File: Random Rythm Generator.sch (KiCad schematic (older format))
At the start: 24 parts, among them SW1 Randomise, U1 LM78L05_TO92, U2 40106, U3 4040, U4 74LS165

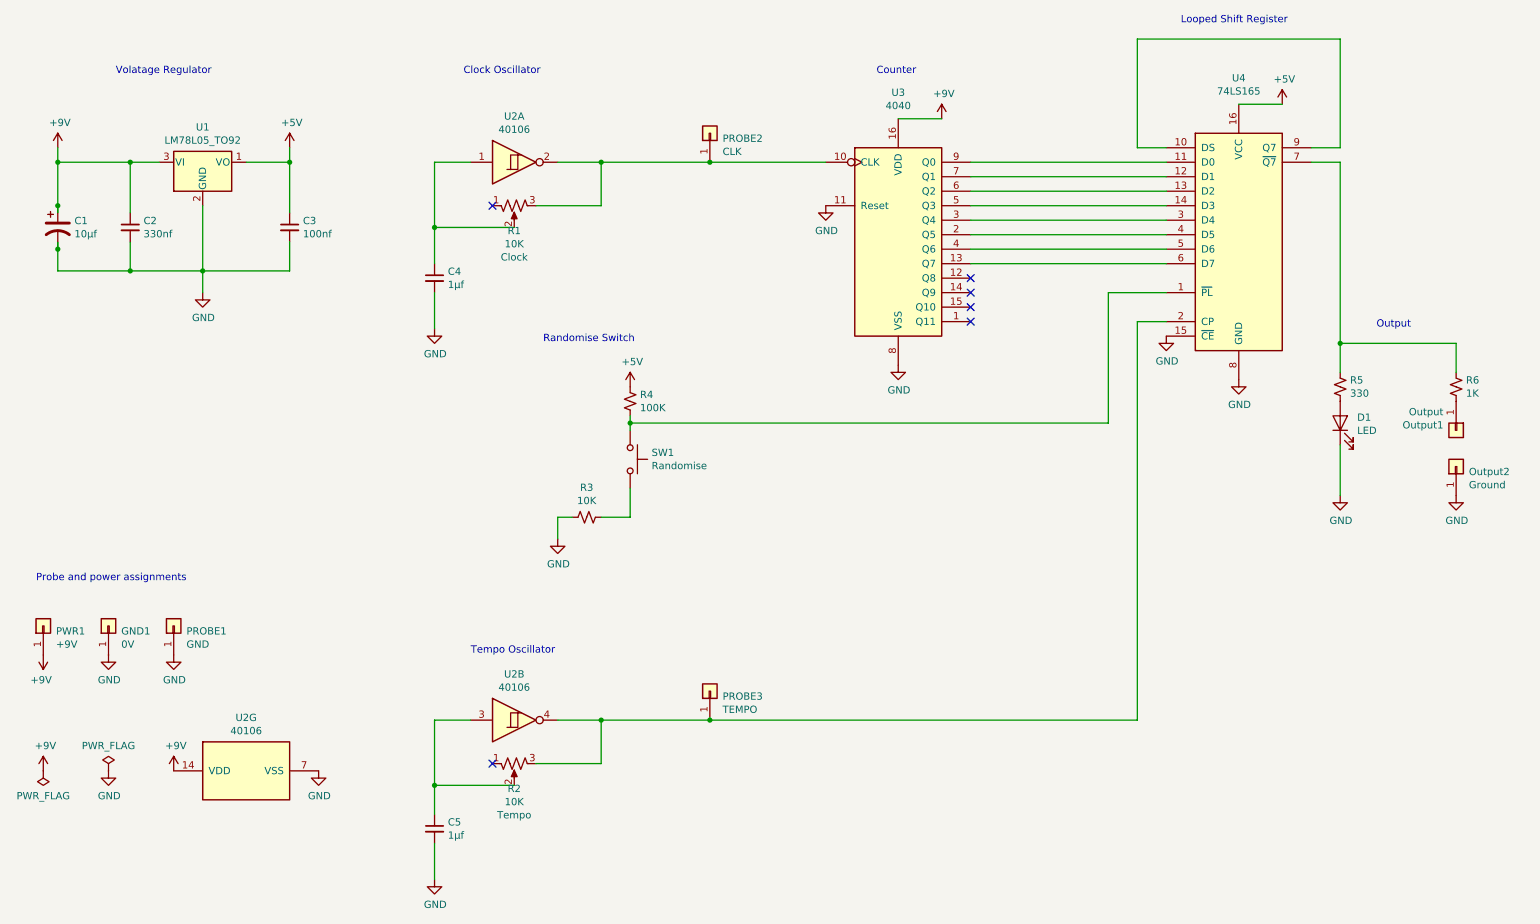
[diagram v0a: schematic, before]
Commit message: add output pins
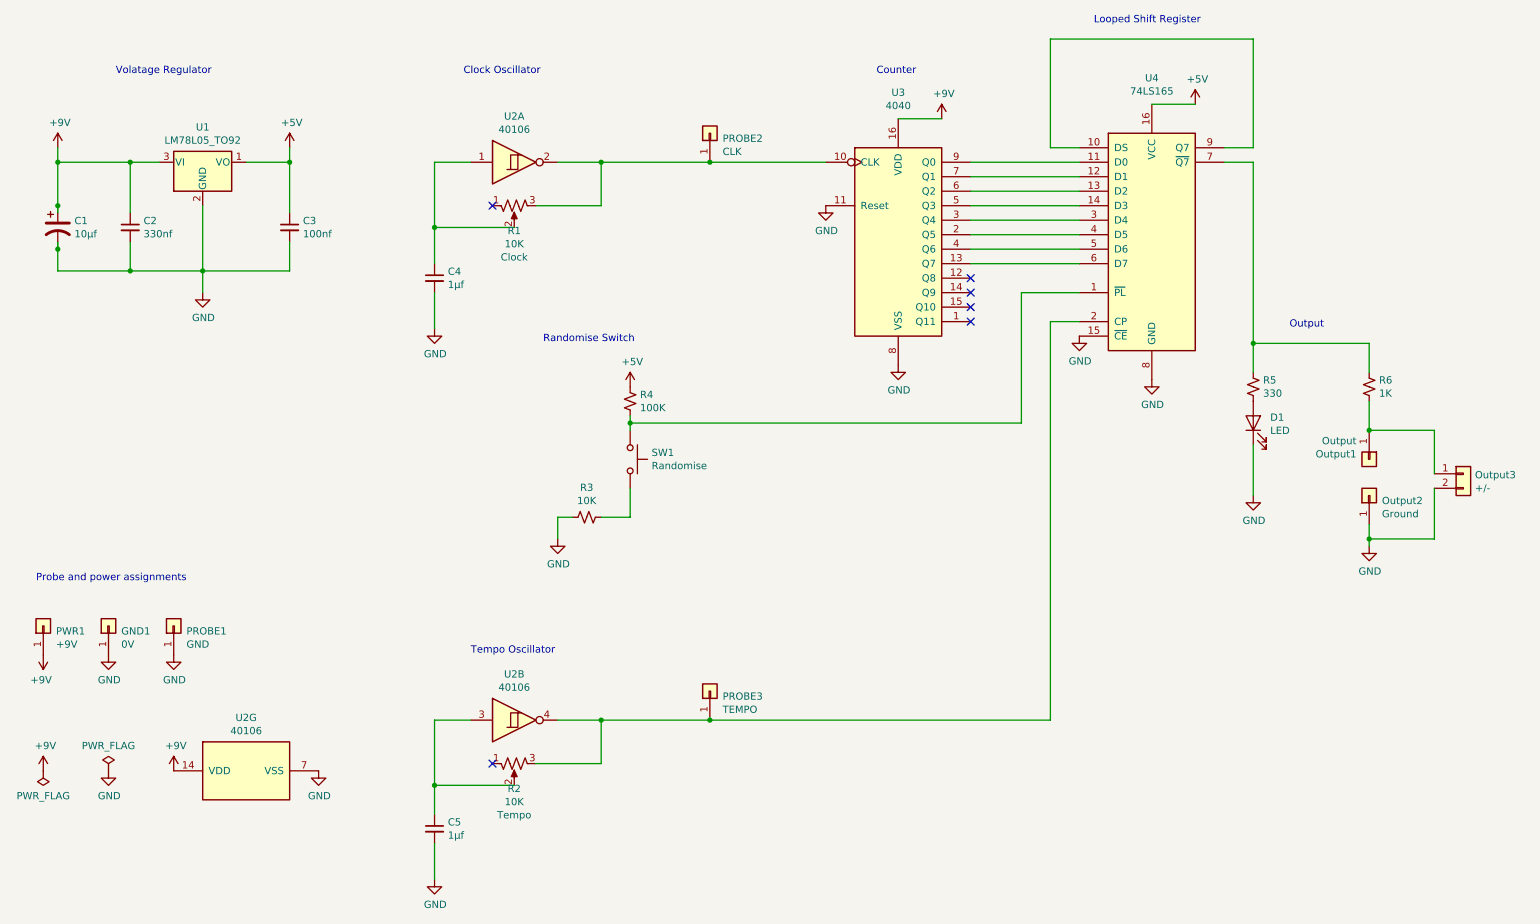
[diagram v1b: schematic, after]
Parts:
- added Output3: +/-, Connector_PinHeader_2.54mm:PinHeader_1x02_P2.54mm_Vertical, symbol Connector_Generic:Conn_01x02
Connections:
- wire segments 70 -> 77
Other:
- moved on the sheet: D1, Output1, Output2, R5, R6, U4
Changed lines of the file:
@@
 	3550 6650 3550 6900
 Wire Wire Line
-	7250 1950 8600 1950
-Wire Wire Line
-	8600 2050 7250 2050
-Wire Wire Line
-	7250 2150 8600 2150
-Wire Wire Line
-	7250 2250 8600 2250
-Wire Wire Line
-	8600 2350 7250 2350
-Wire Wire Line
-	8600 2550 7250 2550
-Wire Wire Line
-	7250 2650 8600 2650
+	7250 1950 8000 1950
+Wire Wire Line
+	8000 2050 7250 2050
+Wire Wire Line
+	7250 2150 8000 2150
+Wire Wire Line
+	7250 2250 8000 2250
+Wire Wire Line
+	8000 2350 7250 2350
+Wire Wire Line
+	8000 2550 7250 2550
+Wire Wire Line
+	7250 2650 8000 2650
 $Comp
 L power:+5V #PWR020
 U 1 1 5D24E019
-P 9400 1550
-F 0 "#PWR020" H 9400 1400 50  0001 C CNN
-F 1 "+5V" H 9415 1723 50  0000 C CNN
-F 2 "" H 9400 1550 50  0001 C CNN
-F 3 "" H 9400 1550 50  0001 C CNN
-	1    9400 1550
-	1    0    0    -1
-$EndComp
-Wire Wire Line
-	9100 1550 9400 1550
+P 8800 1550
+F 0 "#PWR020" H 8800 1400 50  0001 C CNN
+F 1 "+5V" H 8815 1723 50  0000 C CNN
+F 2 "" H 8800 1550 50  0001 C CNN
+F 3 "" H 8800 1550 50  0001 C CNN
+	1    8800 1550
+	1    0    0    -1
+$EndComp
+Wire Wire Line
+	8500 1550 8800 1550
 Wire Wire Line
 	6250 1950 5450 1950
@@
 	4900 4400 4700 4400
 Wire Wire Line
-	8200 2850 8600 2850
-Wire Wire Line
-	8600 3050 8400 3050
-Wire Wire Line
-	8400 3050 8400 5800
-Wire Wire Line
-	8400 5800 5450 5800
+	7600 2850 8000 2850
+Wire Wire Line
+	8000 3050 7800 3050
+Wire Wire Line
+	7800 3050 7800 5800
+Wire Wire Line
+	7800 5800 5450 5800
 Connection ~ 4700 5800
 $Comp
 L 74xx:74LS165 U4
 U 1 1 5D23B4A8
-P 9100 2450
-F 0 "U4" H 9100 3531 50  0000 C CNN
-F 1 "74LS165" H 9100 3440 50  0000 C CNN
-F 2 "Package_DIP:DIP-16_W7.62mm" H 9100 2450 50  0001 C CNN
-F 3 "http://www.ti.com/lit/gpn/sn74LS165" H 9100 2450 50  0001 C CNN
-	1    9100 2450
-	1    0    0    -1
-$EndComp
-Wire Wire Line
-	8200 3750 4900 3750
+P 8500 2450
+F 0 "U4" H 8500 3531 50  0000 C CNN
+F 1 "74LS165" H 8500 3440 50  0000 C CNN
+F 2 "Package_DIP:DIP-16_W7.62mm" H 8500 2450 50  0001 C CNN
+F 3 "http://www.ti.com/lit/gpn/sn74LS165" H 8500 2450 50  0001 C CNN
+	1    8500 2450
+	1    0    0    -1
+$EndComp
+Wire Wire Line
+	7600 3750 4900 3750
 Wire Wire Line
 	4900 3700 4900 3750
@@
 $EndComp
 Wire Wire Line
-	8200 2850 8200 3750
+	7600 2850 7600 3750
 $Comp
 L power:GND #PWR016
@@
 L power:GND #PWR018
 U 1 1 5D2D3DCC
-P 8600 3150
-F 0 "#PWR018" H 8600 2900 50  0001 C CNN
-F 1 "GND" H 8605 2977 50  0000 C CNN
-F 2 "" H 8600 3150 50  0001 C CNN
-F 3 "" H 8600 3150 50  0001 C CNN
-	1    8600 3150
-	1    0    0    -1
-$EndComp
-Wire Wire Line
-	8600 1850 8400 1850
-Wire Wire Line
-	8400 1850 8400 1100
-Wire Wire Line
-	8400 1100 9800 1100
-Wire Wire Line
-	9800 1100 9800 1850
-Wire Wire Line
-	9800 1850 9600 1850
+P 8000 3150
+F 0 "#PWR018" H 8000 2900 50  0001 C CNN
+F 1 "GND" H 8005 2977 50  0000 C CNN
+F 2 "" H 8000 3150 50  0001 C CNN
+F 3 "" H 8000 3150 50  0001 C CNN
+	1    8000 3150
+	1    0    0    -1
+$EndComp
+Wire Wire Line
+	8000 1850 7800 1850
+Wire Wire Line
+	7800 1850 7800 1100
+Wire Wire Line
+	7800 1100 9200 1100
+Wire Wire Line
+	9200 1100 9200 1850
+Wire Wire Line
+	9200 1850 9000 1850
 Text Notes 3800 5350 0    50   ~ 0
 Tempo Oscillator
@@
 	5450 5800 4700 5800
 Wire Wire Line
-	9800 1950 9600 1950
+	9200 1950 9000 1950
 $Comp
 L Device:R_Small_US R5
 U 1 1 5D29FB9A
-P 9800 3500
-F 0 "R5" H 9868 3546 50  0000 L CNN
-F 1 "330" H 9868 3455 50  0000 L CNN
-F 2 "Resistor_THT:R_Axial_DIN0207_L6.3mm_D2.5mm_P7.62mm_Horizontal" H 9800 3500 50  0001 C CNN
-F 3 "~" H 9800 3500 50  0001 C CNN
-	1    9800 3500
+P 9200 3500
+F 0 "R5" H 9268 3546 50  0000 L CNN
+F 1 "330" H 9268 3455 50  0000 L CNN
+F 2 "Resistor_THT:R_Axial_DIN0207_L6.3mm_D2.5mm_P7.62mm_Horizontal" H 9200 3500 50  0001 C CNN
+F 3 "~" H 9200 3500 50  0001 C CNN
+	1    9200 3500
 	1    0    0    -1
 $EndComp
@@
 L Device:LED D1
 U 1 1 5D2A12B9
-P 9800 3750
-F 0 "D1" V 9839 3633 50  0000 R CNN
-F 1 "LED" V 9748 3633 50  0000 R CNN
-F 2 "LED_THT:LED_D3.0mm" H 9800 3750 50  0001 C CNN
-F 3 "~" H 9800 3750 50  0001 C CNN
-	1    9800 3750
+P 9200 3750
+F 0 "D1" V 9239 3633 50  0000 R CNN
+F 1 "LED" V 9148 3633 50  0000 R CNN
+F 2 "LED_THT:LED_D3.0mm" H 9200 3750 50  0001 C CNN
+F 3 "~" H 9200 3750 50  0001 C CNN
+	1    9200 3750
 	0    -1   -1   0
 $EndComp
 Wire Wire Line
-	9800 4250 9800 3900
+	9200 4250 9200 3900
 $Comp
 L power:GND #PWR021
 U 1 1 5D2D6A39
-P 9800 4250
-F 0 "#PWR021" H 9800 4000 50  0001 C CNN
-F 1 "GND" H 9805 4077 50  0000 C CNN
-F 2 "" H 9800 4250 50  0001 C CNN
-F 3 "" H 9800 4250 50  0001 C CNN
-	1    9800 4250
-	1    0    0    -1
-$EndComp
-Wire Wire Line
-	7250 2450 8600 2450
+P 9200 4250
+F 0 "#PWR021" H 9200 4000 50  0001 C CNN
+F 1 "GND" H 9205 4077 50  0000 C CNN
+F 2 "" H 9200 4250 50  0001 C CNN
+F 3 "" H 9200 4250 50  0001 C CNN
+	1    9200 4250
+	1    0    0    -1
+$EndComp
+Wire Wire Line
+	7250 2450 8000 2450
 $Comp
 L 4xxx:4040 U3
@@
 L power:GND #PWR019
 U 1 1 5D2F557C
-P 9100 3450
-F 0 "#PWR019" H 9100 3200 50  0001 C CNN
-F 1 "GND" H 9105 3277 50  0000 C CNN
-F 2 "" H 9100 3450 50  0001 C CNN
-F 3 "" H 9100 3450 50  0001 C CNN
-	1    9100 3450
+P 8500 3450
+F 0 "#PWR019" H 8500 3200 50  0001 C CNN
+F 1 "GND" H 8505 3277 50  0000 C CNN
+F 2 "" H 8500 3450 50  0001 C CNN
+F 3 "" H 8500 3450 50  0001 C CNN
+	1    8500 3450
 	1    0    0    -1
 $EndComp
@@
 	1    0    0    -1
 $EndComp
-Text Notes 8700 1000 0    50   ~ 0
+Text Notes 8100 1000 0    50   ~ 0
 Looped Shift Register
 $Comp
@@
 Text Notes 4300 3200 0    50   ~ 0
 Randomise Switch
-Connection ~ 9800 3200
-Wire Wire Line
-	9800 3200 9800 3400
-Wire Wire Line
-	9800 1950 9800 3200
-Wire Wire Line
-	9800 3200 10600 3200
-$Comp
-L power:GND #PWR022
-U 1 1 5D231795
-P 10600 4250
-F 0 "#PWR022" H 10600 4000 50  0001 C CNN
-F 1 "GND" H 10605 4077 50  0000 C CNN
-F 2 "" H 10600 4250 50  0001 C CNN
-F 3 "" H 10600 4250 50  0001 C CNN
-	1    10600 4250
-	1    0    0    -1
-$EndComp
-$Comp
-L Connector_Generic:Conn_01x01 Output2
-U 1 1 5D22ECC4
-P 10600 4050
-F 0 "Output2" V 10564 3962 50  0000 R CNN
-F 1 "Ground" V 10473 3962 50  0000 R CNN
-F 2 "TestPoint:TestPoint_THTPad_2.5x2.5mm_Drill1.2mm" H 10600 4050 50  0001 C CNN
-F 3 "~" H 10600 4050 50  0001 C CNN
-	1    10600 4050
-	0    -1   -1   0
-$EndComp
-$Comp
-L Connector_Generic:Conn_01x01 Output1
-U 1 1 5D22DC94
-P 10600 3800
-F 0 "Output1" V 10564 3712 50  0000 R CNN
-F 1 "Output" V 10473 3712 50  0000 R CNN
-F 2 "TestPoint:TestPoint_THTPad_2.5x2.5mm_Drill1.2mm" H 10600 3800 50  0001 C CNN
-F 3 "~" H 10600 3800 50  0001 C CNN
-	1    10600 3800
-	0    1    1    0
-$EndComp
-Wire Wire Line
-	10600 3400 10600 3200
-$Comp
-L Device:R_Small_US R6
-U 1 1 5D22A0E3
-P 10600 3500
-F 0 "R6" H 10668 3546 50  0000 L CNN
-F 1 "1K" H 10668 3455 50  0000 L CNN
-F 2 "Resistor_THT:R_Axial_DIN0207_L6.3mm_D2.5mm_P7.62mm_Horizontal" H 10600 3500 50  0001 C CNN
-F 3 "~" H 10600 3500 50  0001 C CNN
-	1    10600 3500
-	1    0    0    -1
-$EndComp
-Text Notes 10050 3100 0    50   ~ 0
+Connection ~ 9200 3200
+Wire Wire Line
+	9200 3200 9200 3400
+Wire Wire Line
+	9200 1950 9200 3200
+Text Notes 9450 3100 0    50   ~ 0
 Output
 $Comp
@@
 Wire Wire Line
 	6750 1650 7050 1650
+Wire Wire Line
+	9200 3200 10000 3200
+Wire Wire Line
+	10000 3400 10000 3200
+$Comp
+L Device:R_Small_US R6
+U 1 1 5D22A0E3
+P 10000 3500
+F 0 "R6" H 10068 3546 50  0000 L CNN
+F 1 "1K" H 10068 3455 50  0000 L CNN
+F 2 "Resistor_THT:R_Axial_DIN0207_L6.3mm_D2.5mm_P7.62mm_Horizontal" H 10000 3500 50  0001 C CNN
+F 3 "~" H 10000 3500 50  0001 C CNN
+	1    10000 3500
+	1    0    0    -1
+$EndComp
+$Comp
+L power:GND #PWR022
+U 1 1 5D231795
+P 10000 4600
+F 0 "#PWR022" H 10000 4350 50  0001 C CNN
+F 1 "GND" H 10005 4427 50  0000 C CNN
+F 2 "" H 10000 4600 50  0001 C CNN
+F 3 "" H 10000 4600 50  0001 C CNN
+	1    10000 4600
+	1    0    0    -1
+$EndComp
+$Comp
+L Connector_Generic:Conn_01x01 Output2
+U 1 1 5D22ECC4
+P 10000 4250
+F 0 "Output2" V 9964 4162 50  0000 R CNN
+F 1 "Ground" V 9873 4162 50  0000 R CNN
+F 2 "TestPoint:TestPoint_THTPad_2.5x2.5mm_Drill1.2mm" H 10000 4250 50  0001 C CNN
+F 3 "~" H 10000 4250 50  0001 C CNN
+	1    10000 4250
+	0    -1   -1   0
+$EndComp
+$Comp
+L Connector_Generic:Conn_01x01 Output1
+U 1 1 5D22DC94
+P 10000 4000
+F 0 "Output1" V 9964 3912 50  0000 R CNN
+F 1 "Output" V 9873 3912 50  0000 R CNN
+F 2 "TestPoint:TestPoint_THTPad_2.5x2.5mm_Drill1.2mm" H 10000 4000 50  0001 C CNN
+F 3 "~" H 10000 4000 50  0001 C CNN
+	1    10000 4000
+	0    1    1    0
+$EndComp
+Wire Wire Line
+	10000 3800 10000 3600
+$Comp
+L Connector_Generic:Conn_01x02 Output3
+U 1 1 5D24381C
+P 10650 4100
+F 0 "Output3" H 10730 4092 50  0000 L CNN
+F 1 "+/-" H 10730 4001 50  0000 L CNN
+F 2 "Connector_PinHeader_2.54mm:PinHeader_1x02_P2.54mm_Vertical" H 10650 4100 50  0001 C CNN
+F 3 "~" H 10650 4100 50  0001 C CNN
+	1    10650 4100
+	1    0    0    -1
+$EndComp
+Wire Wire Line
+	10450 4100 10450 3800
+Wire Wire Line
+	10450 3800 10000 3800
+Connection ~ 10000 3800
+Wire Wire Line
+	10000 4450 10000 4550
+Wire Wire Line
+	10450 4200 10450 4550
+Wire Wire Line
+	10450 4550 10000 4550
+Connection ~ 10000 4550
+Wire Wire Line
+	10000 4550 10000 4600
 $EndSCHEMATC

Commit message: fix chip power supply by swapping vdd and vss
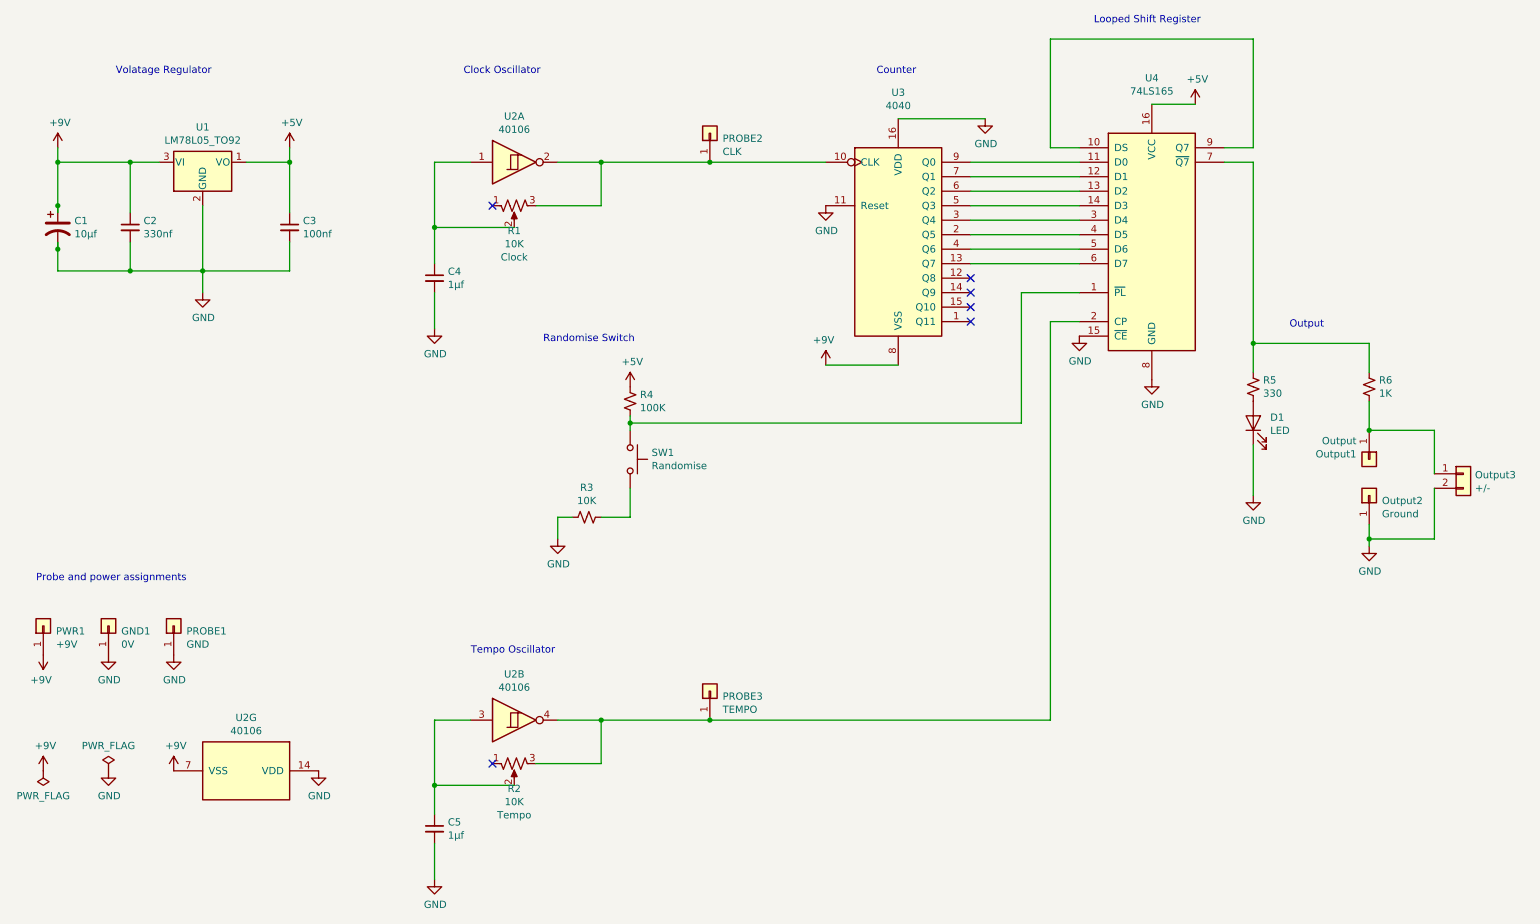
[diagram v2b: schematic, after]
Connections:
- net +9V: now also U2.7 (VSS), U3.8 (VSS); no longer U2.14 (VDD), U3.16 (VDD)
- net GND: now also U2.14 (VDD), U3.16 (VDD); no longer U2.7 (VSS), U3.8 (VSS)
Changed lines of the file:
@@
 Title "Random Rhythm Generator"
 Date "2019-07-05"
-Rev "0.1a"
+Rev "0.1-pre"
 Comp "TBA"
 Comment1 ""
@@
 $EndComp
 Wire Wire Line
-	7600 3750 4900 3750
-Wire Wire Line
 	4900 3700 4900 3750
 Connection ~ 4900 3750
@@
 	1950 2700 2550 2700
 $Comp
-L power:GND #PWR012
-U 1 1 5D2CC067
-P 3550 6900
-F 0 "#PWR012" H 3550 6650 50  0001 C CNN
-F 1 "GND" H 3555 6727 50  0000 C CNN
-F 2 "" H 3550 6900 50  0001 C CNN
-F 3 "" H 3550 6900 50  0001 C CNN
-	1    3550 6900
-	1    0    0    -1
-$EndComp
-$Comp
 L power:GND #PWR013
 U 1 1 5D2CC7A8
@@
 Wire Wire Line
 	7600 2850 7600 3750
-$Comp
-L power:GND #PWR016
-U 1 1 5D2D2858
-P 6750 3350
-F 0 "#PWR016" H 6750 3100 50  0001 C CNN
-F 1 "GND" H 6755 3177 50  0000 C CNN
-F 2 "" H 6750 3350 50  0001 C CNN
-F 3 "" H 6750 3350 50  0001 C CNN
-	1    6750 3350
-	1    0    0    -1
-$EndComp
 $Comp
 L power:GND #PWR018
@@
 Wire Wire Line
 	9200 4250 9200 3900
-$Comp
-L power:GND #PWR021
-U 1 1 5D2D6A39
-P 9200 4250
-F 0 "#PWR021" H 9200 4000 50  0001 C CNN
-F 1 "GND" H 9205 4077 50  0000 C CNN
-F 2 "" H 9200 4250 50  0001 C CNN
-F 3 "" H 9200 4250 50  0001 C CNN
-	1    9200 4250
-	1    0    0    -1
-$EndComp
 Wire Wire Line
 	7250 2450 8000 2450
@@
 L power:+9V #PWR017
 U 1 1 5D328148
-P 7050 1650
-F 0 "#PWR017" H 7050 1500 50  0001 C CNN
-F 1 "+9V" H 7065 1823 50  0000 C CNN
-F 2 "" H 7050 1650 50  0001 C CNN
-F 3 "" H 7050 1650 50  0001 C CNN
-	1    7050 1650
-	1    0    0    -1
+P 6250 3350
+F 0 "#PWR017" H 6250 3200 50  0001 C CNN
+F 1 "+9V" H 6265 3523 50  0000 C CNN
+F 2 "" H 6250 3350 50  0001 C CNN
+F 3 "" H 6250 3350 50  0001 C CNN
+	1    6250 3350
+	-1   0    0    -1
 $EndComp
 Text Notes 8100 1000 0    50   ~ 0
@@
 F 3 "https://assets.nexperia.com/documents/data-sheet/HEF40106B.pdf" H 2250 6150 50  0001 C CNN
 	7    2250 6150
-	0    -1   1    0
-$EndComp
-$Comp
-L power:GND #PWR010
-U 1 1 5D308744
-P 2750 6150
-F 0 "#PWR010" H 2750 5900 50  0001 C CNN
-F 1 "GND" H 2755 5977 50  0000 C CNN
-F 2 "" H 2750 6150 50  0001 C CNN
-F 3 "" H 2750 6150 50  0001 C CNN
-	1    2750 6150
-	1    0    0    -1
+	0    1    1    0
 $EndComp
 $Comp
@@
 $EndComp
 Wire Wire Line
-	6750 1650 7050 1650
-Wire Wire Line
 	9200 3200 10000 3200
 Wire Wire Line
@@
 Wire Wire Line
 	10000 4550 10000 4600
+Wire Wire Line
+	4900 3750 7600 3750
+Wire Wire Line
+	6750 3350 6250 3350
+Wire Wire Line
+	7350 1650 6750 1650
+$Comp
+L power:GND #PWR0103
+U 1 1 5D25B4F3
+P 2750 6150
+F 0 "#PWR0103" H 2750 5900 50  0001 C CNN
+F 1 "GND" H 2755 5977 50  0000 C CNN
+F 2 "" H 2750 6150 50  0001 C CNN
+F 3 "" H 2750 6150 50  0001 C CNN
+	1    2750 6150
+	1    0    0    -1
+$EndComp
+$Comp
+L power:GND #PWR0101
+U 1 1 5D25EC97
+P 7350 1650
+F 0 "#PWR0101" H 7350 1400 50  0001 C CNN
+F 1 "GND" H 7355 1477 50  0000 C CNN
+F 2 "" H 7350 1650 50  0001 C CNN
+F 3 "" H 7350 1650 50  0001 C CNN
+	1    7350 1650
+	1    0    0    -1
+$EndComp
+$Comp
+L power:GND #PWR?
+U 1 1 5D2611FF
+P 3550 6900
+F 0 "#PWR?" H 3550 6650 50  0001 C CNN
+F 1 "GND" H 3555 6727 50  0000 C CNN
+F 2 "" H 3550 6900 50  0001 C CNN
+F 3 "" H 3550 6900 50  0001 C CNN
+	1    3550 6900
+	1    0    0    -1
+$EndComp
+$Comp
+L power:GND #PWR?
+U 1 1 5D261A64
+P 9200 4250
+F 0 "#PWR?" H 9200 4000 50  0001 C CNN
+F 1 "GND" H 9205 4077 50  0000 C CNN
+F 2 "" H 9200 4250 50  0001 C CNN
+F 3 "" H 9200 4250 50  0001 C CNN
+	1    9200 4250
+	1    0    0    -1
+$EndComp
 $EndSCHEMATC
